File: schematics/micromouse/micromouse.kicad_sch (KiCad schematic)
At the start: 36 parts, among them J1 TOF_LEFT, J10 MotorB_Conn, J11 BMI_ConnB, J12 BMI_ConnA, J13 StepDown_{In+}, J14 StepDown_{In-}, J15 StepDown_{Out+}, J16 StepDown_{Out-}, J2 TOF_FRONTLEFT, J3 TOF_FRONTRIGHT, J4 TOF_RIGHT, J5 BatteryConnector, J6 PMW3360_Conn, J7 Bluetooth_Conn, J8 Programming_Conn, J9 MotorA_Conn, SW1 SW_Push, SW2 SW_SPDT, U1 STM32F103CBTx, U2 DRV8833PWP, U3 AMS1117-3.3, U4 PCF8574TS, Y1 Crystal (8MHz)

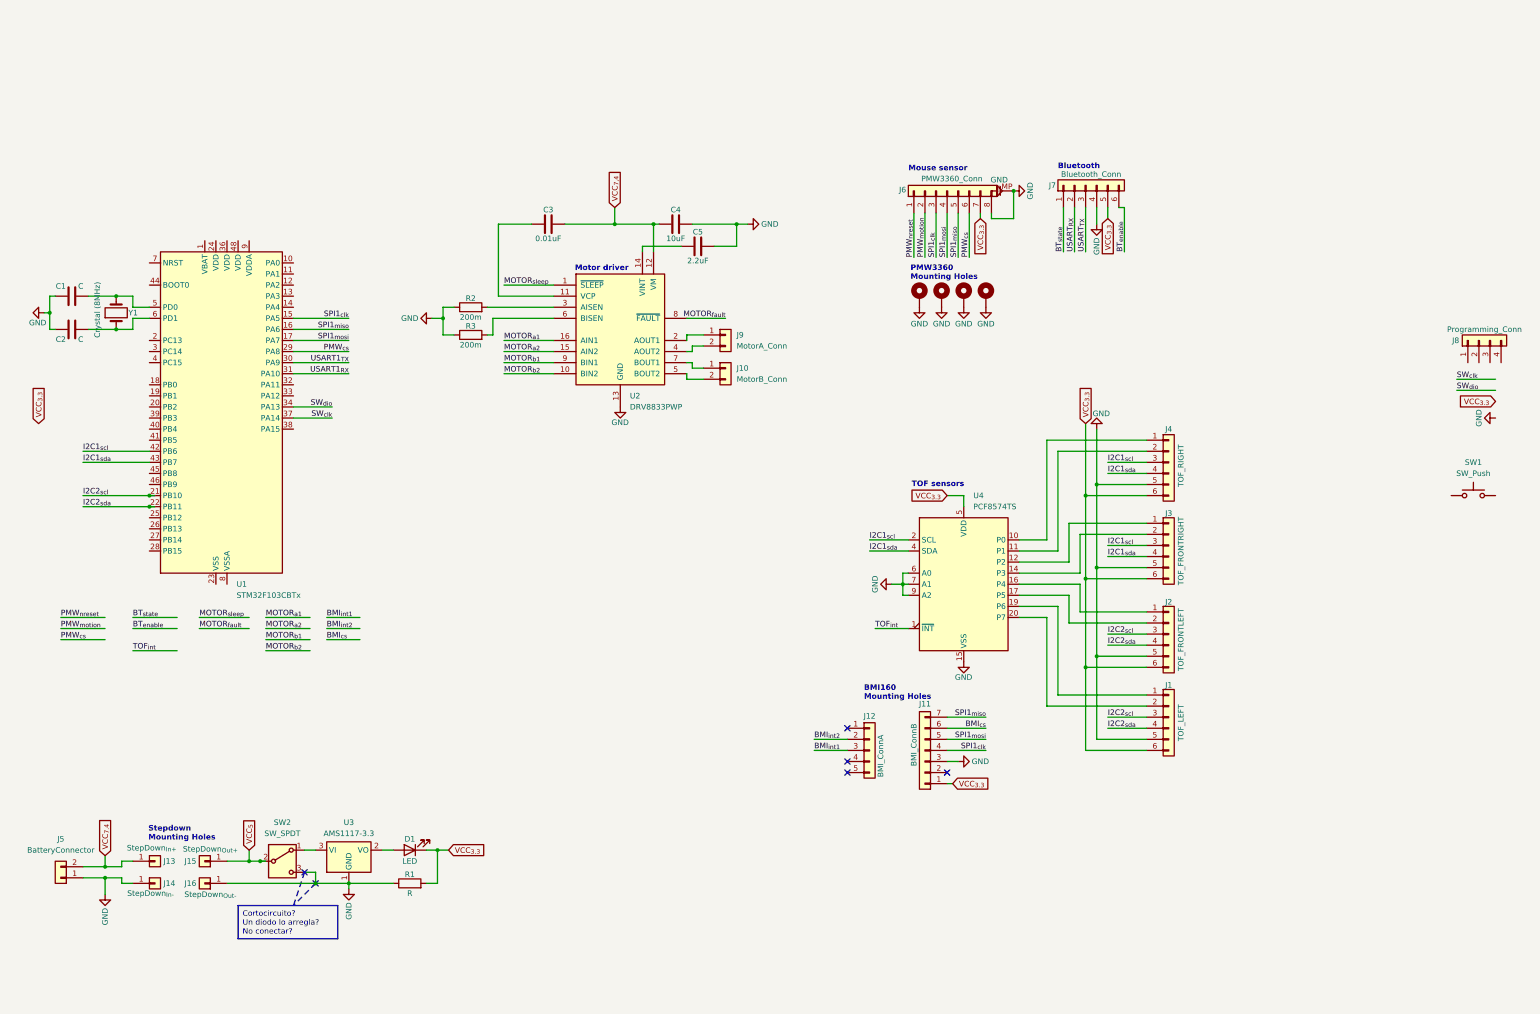
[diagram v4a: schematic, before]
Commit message: Schematic organized in boxes
Schematic status update:
* STM32 with external clock, DebugPort(*) and communication lines (SPI1, I2C0 and I2C1 and USART1, with pull-up resistors in I2C and USART RX lines) and power lines (VDDs and VSSs)
* First version of power supply schematic [TODO: Check possible short circuit]
* Motor controller schematic
* Mouse sensor connector + mounting holes
* Bluetooth connector for HC-05/HC-06
* TOF schematic using GPIO expander
* BMI160 Mounting holes
* DIP Switches
* Reset and Boot circuits
* LEDs for all voltages lines
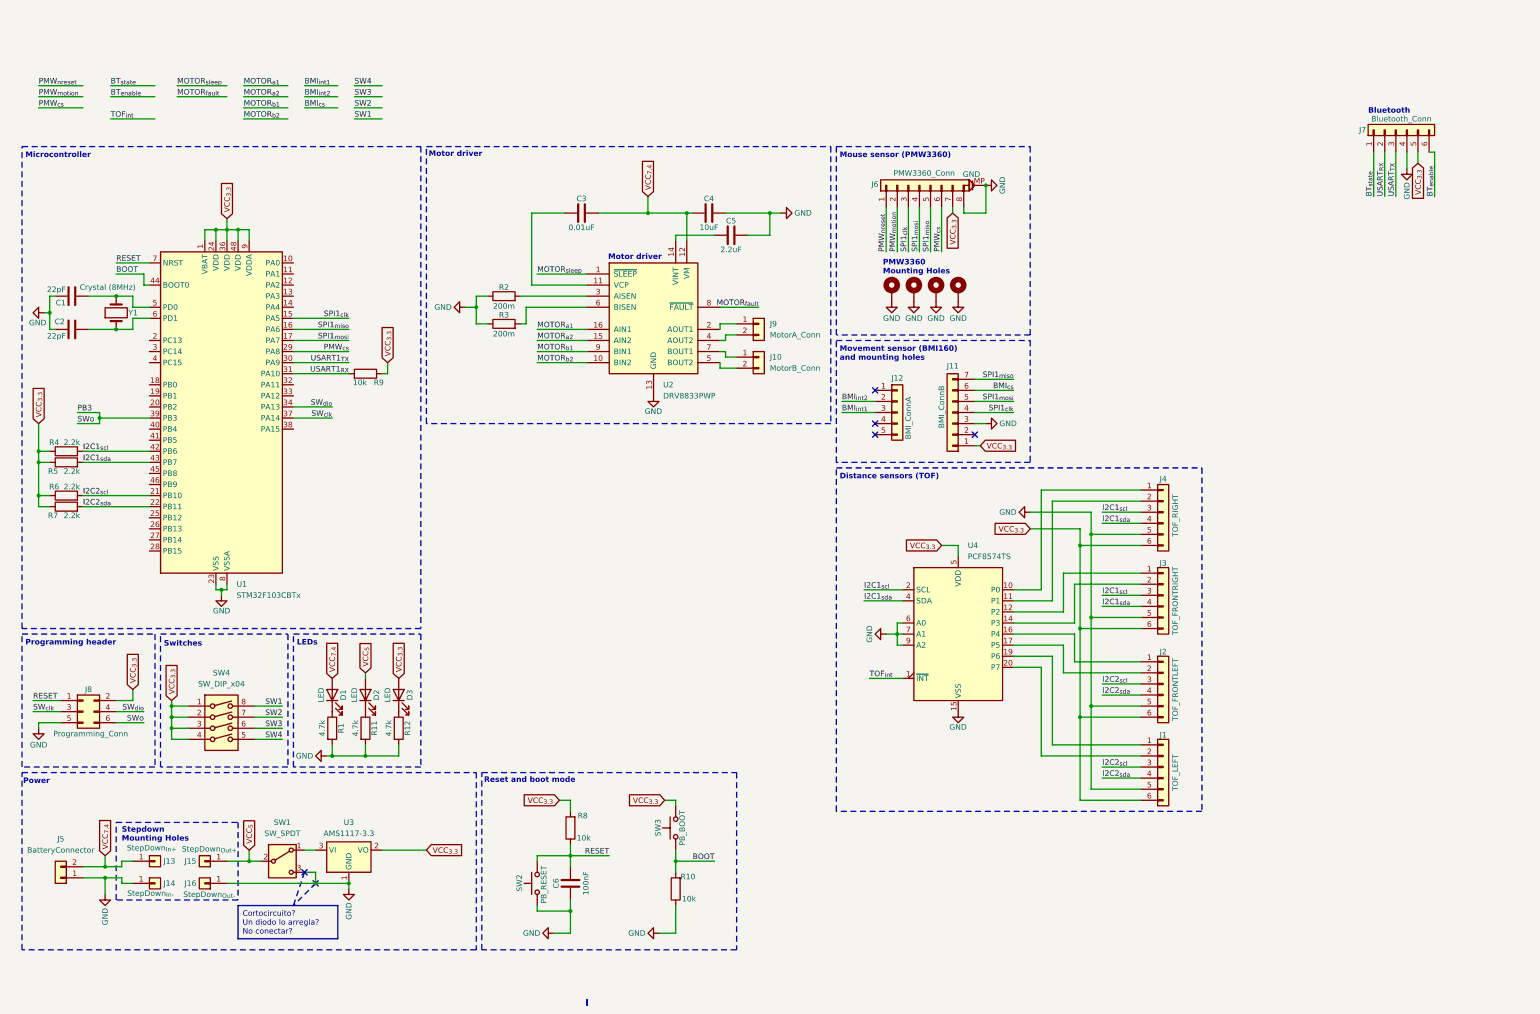
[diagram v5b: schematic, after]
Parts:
- removed SW1: SW_Push, Button_Switch_SMD:SW_SPST_PTS645, symbol Switch:SW_Push
- removed SW2: SW_SPDT, Button_Switch_THT:SW_Slide_SPDT_Straight_CK_OS102011MS2Q, symbol Switch:SW_SPDT
- added C6: 100nF, Capacitor_SMD:C_0805_2012Metric_Pad1.18x1.45mm_HandSolder, symbol Device:C
- added D2, D3: LED, LED_SMD:LED_0805_2012Metric_Pad1.15x1.40mm_HandSolder, symbol Device:LED
- added R10, R8, R9: 10k, Resistor_SMD:R_0805_2012Metric_Pad1.20x1.40mm_HandSolder, symbol Device:R
- added R11, R12: 4.7k, Resistor_SMD:R_0805_2012Metric_Pad1.20x1.40mm_HandSolder, symbol Device:R
- added R4, R5, R6, R7: 2.2k, Resistor_SMD:R_0805_2012Metric_Pad1.20x1.40mm_HandSolder, symbol Device:R
- added SW1: SW_SPDT, Button_Switch_THT:SW_Slide_SPDT_Straight_CK_OS102011MS2Q, symbol Switch:SW_SPDT
- added SW2: PB_RESET, Button_Switch_THT:SW_PUSH_6mm_H5mm, symbol Switch:SW_Push
- added SW3: PB_BOOT, Button_Switch_THT:SW_PUSH_6mm_H5mm, symbol Switch:SW_Push
- added SW4: SW_DIP_x04, Button_Switch_THT:SW_DIP_SPSTx04_Slide_9.78x12.34mm_W7.62mm_P2.54mm, symbol Switch:SW_DIP_x04
- C1, C2: value C -> 22pF
- J8: footprint Connector_PinHeader_2.54mm:PinHeader_1x04_P2.54mm_Vertical -> Connector_PinHeader_2.54mm:PinHeader_2x03_P2.54mm_Vertical; symbol Connector_Generic:Conn_01x04 -> Connector_Generic:Conn_02x03_Odd_Even
- R1: value R -> 4.7k
- Y1: footprint Crystal:Crystal_HC49-4H_Vertical -> Crystal:Crystal_SMD_HC49-SD
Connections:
- net GND: now also J8.5 (Pin_5), R1.2, U1.23 (VSS), U1.35 (VSS), U1.47 (VSS), U1.8 (VSSA), C6.2, R10.1, R11.2, R12.2, SW1.3 (C), SW2.1; no longer R1.1
- net I2C1_{scl}: now also R4.2
- net I2C1_{sda}: now also R5.2
- net I2C2_{scl}: now also R6.2
- net I2C2_{sda}: now also R7.2
- net SW_{clk}: now also J8.3 (Pin_3)
- net SW_{dio}: now also J8.4 (Pin_4)
- net USART1_{RX}: now also R9.2
- net VCC_{3.3}: now also J8.2 (Pin_2), U1.1 (VBAT), U1.24 (VDD), U1.36 (VDD), U1.48 (VDD), U1.9 (VDDA), U3.2 (VO), D3.2 (A), R4.1, R5.1, R6.1, R7.1, R8.2, R9.1, SW3.2, SW4.1, SW4.2, SW4.3, SW4.4; no longer D1.1 (K), R1.2
- net VCC_{5}: now also D2.2 (A), SW1.2 (B)
- net VCC_{7.4}: now also D1.2 (A)
- net at U3.3 (VI): now also SW1.1 (A)
- net PB3: now reaches U1.39 (PB3)
- net PB3: now also J8.6 (Pin_6)
- net BOOT: now reaches U1.44 (BOOT0)
- net BOOT: now also R10.2, SW3.1
- net RESET: now reaches U1.7 (NRST)
- net RESET: now also J8.1 (Pin_1), C6.1, R8.1, SW2.2
- new net: D2.1 (K), R11.1
- new net: D1.1 (K), R1.1
- new net: D3.1 (K), R12.1
- new net SW1: SW4.8
- new net SW2: SW4.7
- new net SW3: SW4.6
- new net SW4: SW4.5
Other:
- note added: "Distance sensors (TOF)"
- note added: "LEDs"
- note added: "Microcontroller"
- note added: "Mouse sensor (PMW3360)"
- note added: "Movement sensor (BMI160) and mounting holes"
- note added: "Power"
- note added: "Programming header"
- note added: "Reset and boot mode"
- note added: "Switches"
- note removed: "BMI160 Mounting Holes"
- note removed: "Mouse sensor"
- note removed: "TOF sensors"
- moved on the sheet: C3, C4, C5, J1, J10, J11, J12, J2, J3, J4, J6, J7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

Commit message: Schematic status: * STM32 with external clock, DebugPort(*) and communication lines (SPI1, I2C1 and I2C2 and USART1, with pull-up resistors in I2C and USART RX lines) and power lines (VDDs and VSSs) * Motor driver with encoders connections * Programming header * Bluetooth/USART connector * Power LED indicators * Power supply * Reset and boot mode buttons * Mouse sensor with mounting holes * Flash memory (SPI nor flash) * Accelerometer+Gyro mounting holes * Distance sensors (GPIO expander + TOF connectors) * User LEDs and switches (GPIO expander + 4x LEDs + 4x switches)
PCB:
* Reorganized pcb board to use space below motors

ToDo:
* Connect signals to the microcontroller in the schematic (signals are listed in priority order at the top)
* Create tracks and planes in the PCB
* Validate the design
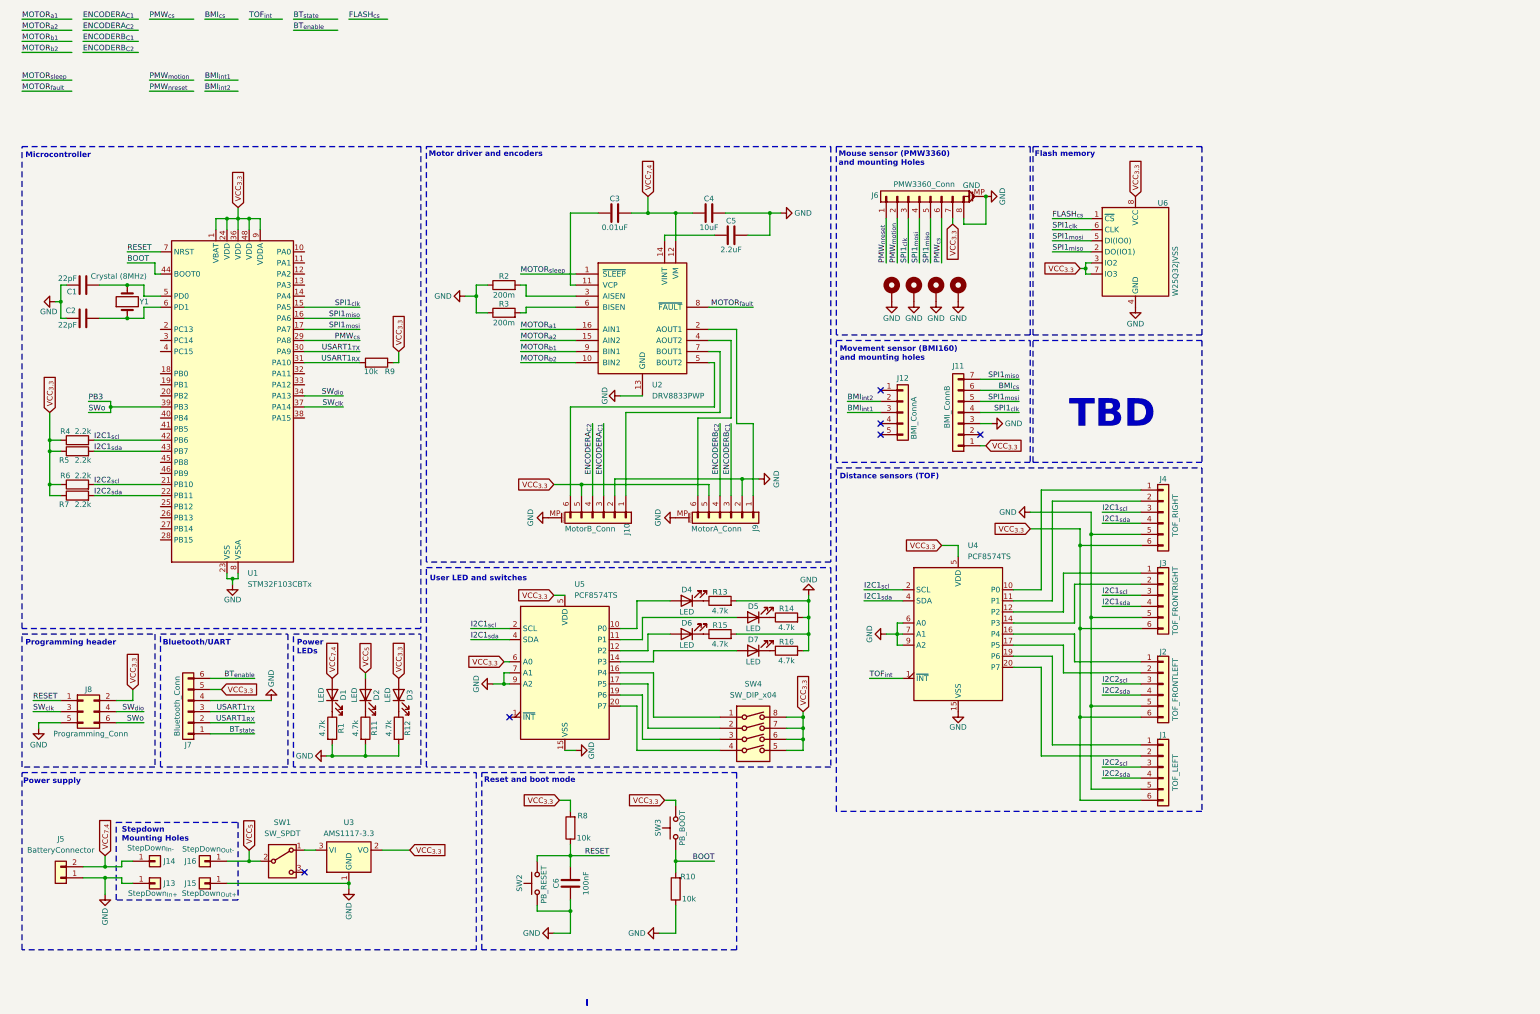
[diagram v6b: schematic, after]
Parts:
- removed J10: MotorB_Conn, Connector_JST:JST_EH_B2B-EH-A_1x02_P2.50mm_Vertical, symbol Connector_Generic:Conn_01x02
- removed J9: MotorA_Conn, Connector_JST:JST_EH_B2B-EH-A_1x02_P2.50mm_Vertical, symbol Connector_Generic:Conn_01x02
- added D4, D5, D6, D7: LED, LED_SMD:LED_0805_2012Metric_Pad1.15x1.40mm_HandSolder, symbol Device:LED
- added J10: MotorB_Conn, Connector_JST:JST_SH_BM06B-SRSS-TB_1x06-1MP_P1.00mm_Vertical, symbol Connector_Generic_MountingPin:Conn_01x06_MountingPin
- added J9: MotorA_Conn, Connector_JST:JST_SH_BM06B-SRSS-TB_1x06-1MP_P1.00mm_Vertical, symbol Connector_Generic_MountingPin:Conn_01x06_MountingPin
- added R13, R14, R15, R16: 4.7k, Resistor_SMD:R_0805_2012Metric_Pad1.20x1.40mm_HandSolder, symbol Device:R
- added U5: PCF8574TS, Package_SO:SSOP-20_4.4x6.5mm_P0.65mm, symbol Interface_Expansion:PCF8574TS
- added U6: W25Q32JVSS, Package_SO:SOIC-8_5.23x5.23mm_P1.27mm, symbol Memory_Flash:W25Q32JVSS
- J5: footprint Connector_JST:JST_EH_B2B-EH-A_1x02_P2.50mm_Vertical -> Connector_JST:JST_XH_B2B-XH-A_1x02_P2.50mm_Vertical
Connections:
- net SW1 is gone; now on net VCC_{3.3}: SW4.8
- net SW2 is gone; now on net VCC_{3.3}: SW4.7
- net SW3 is gone; now on net VCC_{3.3}: SW4.6
- net SW4 is gone; now on net VCC_{3.3}: SW4.5
- net USART_{RX} is gone; now on net USART1_{RX}: J7.2 (Pin_2)
- net USART_{TX} is gone; now on net USART1_{TX}: J7.3 (Pin_3)
- net GND: now also J13.1 (Pin_1), J15.1 (Pin_1), J10.2 (Pin_2), J10.MP (MountPin), J9.2 (Pin_2), J9.MP (MountPin), R13.2, R14.2, R15.2, R16.2, U5.15 (VSS), U5.7 (A1), U5.9 (A2), U6.4 (GND); no longer J14.1 (Pin_1), J16.1 (Pin_1), SW1.3 (C)
- net I2C1_{scl}: now also U5.2 (SCL)
- net I2C1_{sda}: now also U5.4 (SDA)
- net SPI1_{clk}: now also U6.6 (CLK)
- net SPI1_{miso}: now also U6.2 (DO(IO1))
- net SPI1_{mosi}: now also U6.5 (DI(IO0))
- net VCC_{3.3}: now also J10.5 (Pin_5), J9.5 (Pin_5), U5.5 (VDD), U5.6 (A0), U6.3 (IO2), U6.7 (IO3), U6.8 (VCC); no longer SW4.1, SW4.2, SW4.3, SW4.4
- net VCC_{5}: now also J16.1 (Pin_1); no longer J15.1 (Pin_1)
- net VCC_{7.4}: now also J14.1 (Pin_1); no longer J13.1 (Pin_1)
- net at U2.7 (BOUT1): now also J10.1 (Pin_1)
- net at U2.5 (BOUT2): now also J10.6 (Pin_6)
- net at U2.2 (AOUT1): now also J9.1 (Pin_1)
- net at U2.4 (AOUT2): now also J9.6 (Pin_6)
- new net: D5.1 (K), R14.1
- new net: D5.2 (A), U5.11 (P1)
- new net: D4.1 (K), R13.1
- new net: D6.1 (K), R15.1
- new net: D4.2 (A), U5.10 (P0)
- new net: D6.2 (A), U5.12 (P2)
- new net: D7.2 (A), U5.14 (P3)
- new net: SW4.1, U5.16 (P4)
- new net: SW4.2, U5.17 (P5)
- new net: SW4.3, U5.19 (P6)
- new net: SW4.4, U5.20 (P7)
- new net: D7.1 (K), R16.1
- new net ENCODERA_{C1}: J10.3 (Pin_3)
- new net ENCODERA_{C2}: J10.4 (Pin_4)
- new net ENCODERB_{C1}: J9.3 (Pin_3)
- new net ENCODERB_{C2}: J9.4 (Pin_4)
- new net FLASH_{cs}: U6.1 (~{CS})
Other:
- note added: "Bluetooth/UART"
- note added: "Flash memory"
- note added: "Motor driver and encoders"
- note added: "Mouse sensor (PMW3360) and mounting Holes"
- note added: "Power LEDs"
- note added: "Power supply"
- note added: "TBD"
- note added: "User LED and switches"
- note removed: "Bluetooth"
- note removed: "LEDs"
- note removed: "Motor driver"
- note removed: "Mouse sensor (PMW3360)"
- note removed: "PMW3360 Mounting Holes"
- note removed: "Power"
- note removed: "Switches"
- moved on the sheet: C1, C2, C3, J11, J12, J13, J14, J15, J16, J6, J7, R2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

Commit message: Add second Crystal for second footprint with holes
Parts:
- added Y2: Crystal (8MHz), Crystal:Crystal_HC49-4H_Vertical, symbol Device:Crystal
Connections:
- net BMI_{int2}: now also J12.4 (Pin_4); no longer J12.2 (Pin_2)
- net PMW_{cs}: no longer U1.29 (PA8)
- net at C1.2, U1.5 (PD0), Y1.2: now also Y2.2
- net at C2.1, U1.6 (PD1), Y1.1: now also Y2.1
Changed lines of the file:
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@@
 	)
 	(no_connect
-		(at 209.55 76.2)
+		(at 209.55 78.74)
 	)
 	(no_connect
-		(at 209.55 78.74)
+		(at 209.55 71.12)
 	)
 	(no_connect
@@
 	(wire
 		(pts
-			(xy 77.47 57.15) (xy 90.17 57.15)
-		)
-		(stroke
-			(width 0)
-			(type default)
-		)
-	)
-	(wire
-		(pts
 			(xy 149.86 123.19) (xy 153.67 123.19)
 		)
@@
 	(wire
 		(pts
+			(xy 201.93 76.2) (xy 209.55 76.2)
+		)
+		(stroke
+			(width 0)
+			(type default)
+		)
+	)
+	(wire
+		(pts
 			(xy 59.69 29.21) (xy 62.23 29.21)
 		)
@@
 	(wire
 		(pts
-			(xy 201.93 71.12) (xy 209.55 71.12)
-		)
-		(stroke
-			(width 0)
-			(type default)
-		)
-	)
-	(wire
-		(pts
 			(xy 156.21 146.05) (xy 156.21 135.89)
 		)
@@
 	(rectangle
 		(start 118.11 156.21)
-		(end 176.53 196.85)
+		(end 175.895 196.85)
 		(stroke
 			(width 0)
@@
 		)
 	)
-	(label "BMI_{int2}"
-		(at 201.93 71.12 0)
-		(fields_autoplaced yes)
-		(effects
-			(font
-				(size 1.27 1.27)
-			)
-			(justify left bottom)
-		)
-	)
 	(label "SWo"
 		(at 27.94 73.66 0)
@@
 		)
 	)
-	(label "PMW_{cs}"
-		(at 90.17 57.15 180)
+	(label "I2C1_{sda}"
+		(at 205.74 116.84 0)
 		(fields_autoplaced yes)
 		(effects
@@
 				(size 1.27 1.27)
 			)
-			(justify right bottom)
+			(justify left bottom)
 		)
 	)
-	(label "I2C1_{sda}"
-		(at 205.74 116.84 0)
+	(label "TOF_{int}"
+		(at 207.01 134.62 0)
 		(fields_autoplaced yes)
 		(effects
@@
 		)
 	)
-	(label "TOF_{int}"
-		(at 207.01 134.62 0)
+	(label "BMI_{int2}"
+		(at 201.93 76.2 0)
 		(fields_autoplaced yes)
 		(effects
@@
 		(dnp no)
 		(property "Reference" "Y1"
-			(at 39.624 48.26 90)
+			(at 31.496 47.244 90)
 			(effects
 				(font
@@
 					(unit 1)
 				)
+			)
+		)
+	)
+	(symbol
+		(lib_id "Device:Crystal")
+		(at 36.83 48.26 90)
+		(unit 1)
+		(exclude_from_sim no)
+		(in_bom yes)
+		(on_board yes)
+		(dnp no)
+		(property "Reference" "Y2"
+			(at 31.496 49.022 90)
+			(effects
+				(font
+					(size 1.27 1.27)
+				)
+				(justify right)
+			)
+		)
+		(property "Value" "Crystal (8MHz)"
+			(at 28.448 42.418 90)
+			(effects
+				(font
+					(size 1.27 1.27)
+				)
+				(justify right)
+			)
+		)
+		(property "Footprint" "Crystal:Crystal_HC49-4H_Vertical"
+			(at 36.83 48.26 0)
+			(effects
+				(font
+					(size 1.27 1.27)
+				)
+				(hide yes)
+			)
+		)
+		(property "Datasheet" "~"
+			(at 36.83 48.26 0)
+			(effects
+				(font
+					(size 1.27 1.27)
+				)
+				(hide yes)
+			)
+		)
+		(property "Description" "Two pin crystal"
+			(at 36.83 48.26 0)
+			(effects
+				(font
+					(size 1.27 1.27)
+				)
+				(hide yes)
+			)
+		)
+		(pin "1"
+		)
+		(pin "2"
+		)
+		(instances
+			(project "micromouse"
+				(path "/48923552-97ee-4377-b66c-70fa2ca23716"
+					(reference "Y2")
+					(unit 1)
+				)
